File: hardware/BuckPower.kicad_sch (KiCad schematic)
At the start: 24 parts, among them Q401 NMOS, U401 SIC437A

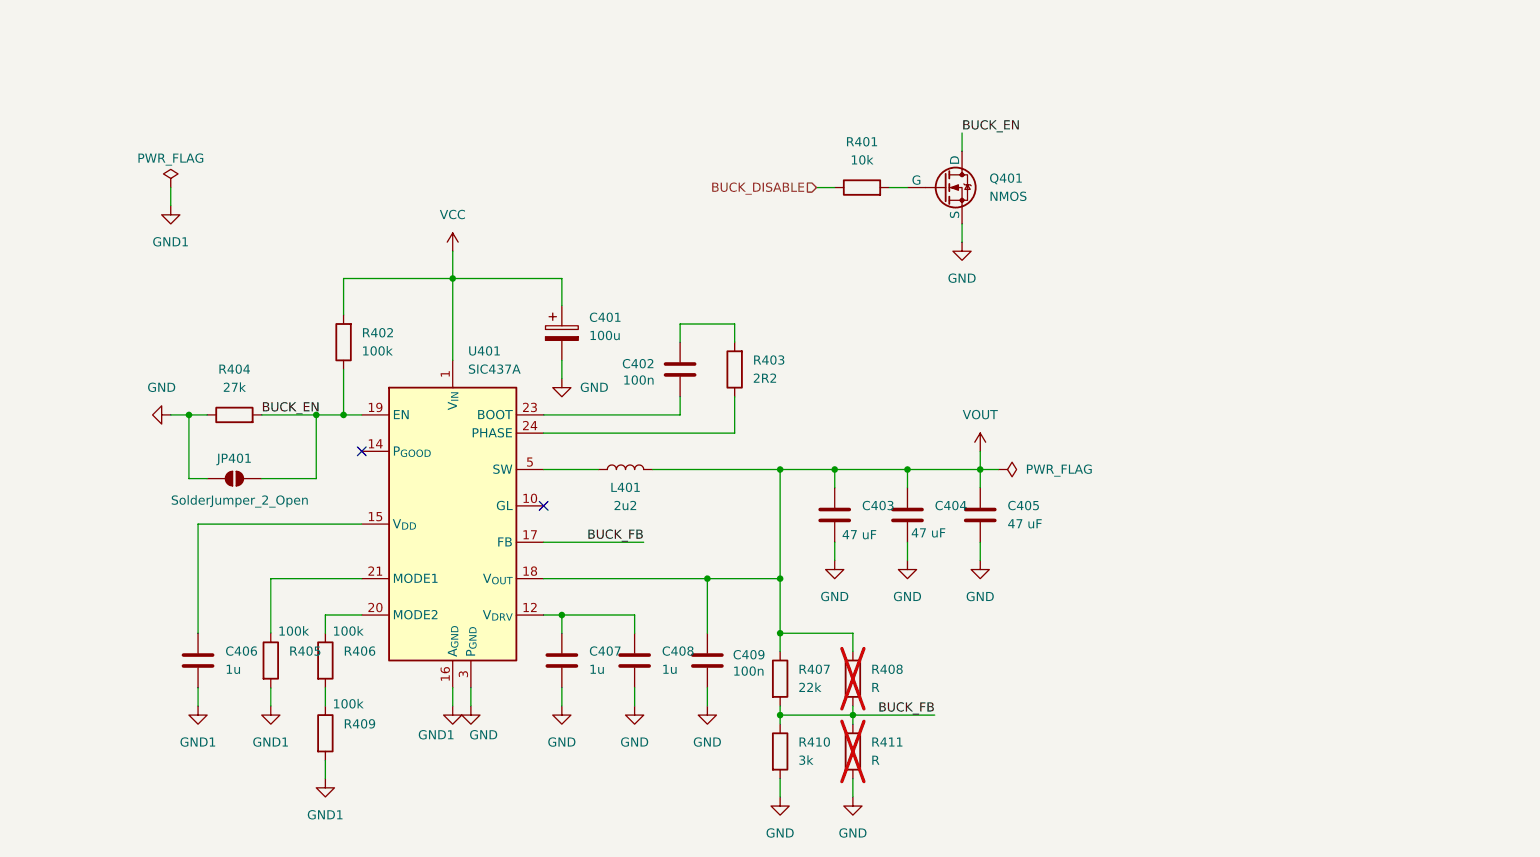
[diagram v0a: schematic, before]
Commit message: Optimized BOM and added netties
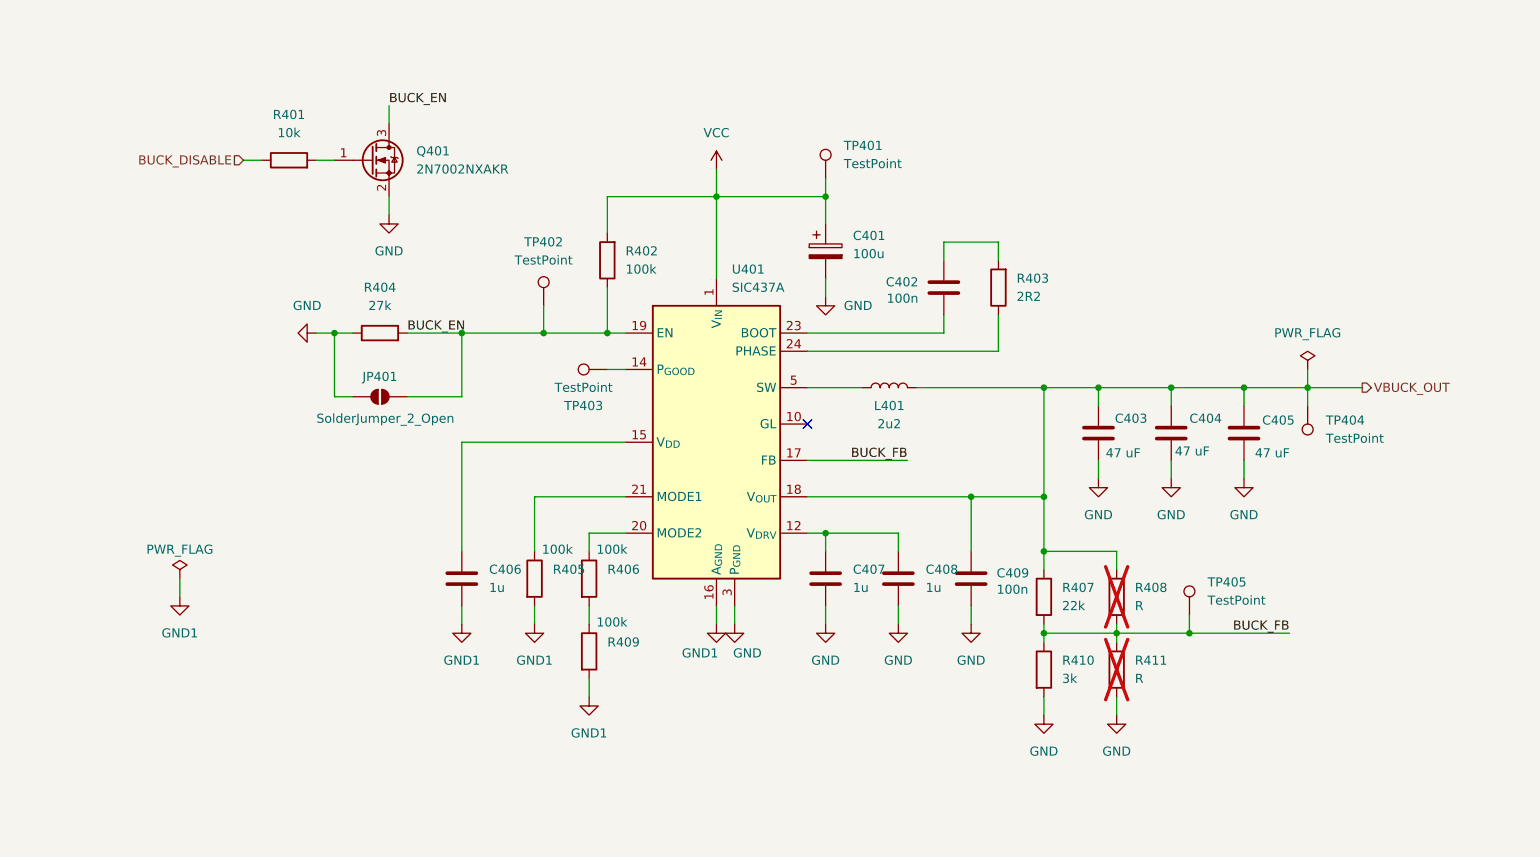
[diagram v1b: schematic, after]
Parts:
- removed Q401: NMOS, symbol Simulation_SPICE:NMOS
- added Q401: 2N7002NXAKR, Package_TO_SOT_SMD:SOT-23-3, symbol glowbuck:2N7002NXAKR
- added TP401, TP402, TP403, TP404, TP405: TestPoint, TestPoint:TestPoint_Pad_D1.0mm, symbol Connector:TestPoint
- L401: footprint (none) -> Inductor_SMD:L_Vishay_IHLP-6767; ManufacturerNumber (none) -> IHLP6767GZER2R2M01; MouserNumber (none) -> 70-IHLP6767GZER2R2M0
- R408, R411: now left out of the parts list
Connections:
- net BUCK_EN: now also Q401.3 (D), TP402.1
- net BUCK_FB: now also TP405.1
- net GND: now also Q401.2 (S)
- net VCC: now also TP401.1
- net at R401.2: now also Q401.1 (G)
- net at U401.14 (P_{GOOD}): now also TP403.1
- net VOUT renamed VBUCK_OUT
- net VBUCK_OUT: now also TP404.1
- no-connect marks 2 -> 1
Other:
- moved on the sheet: C401, C402, C403, C404, C405, C406, C407, C408, C409, JP401, L401, R401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

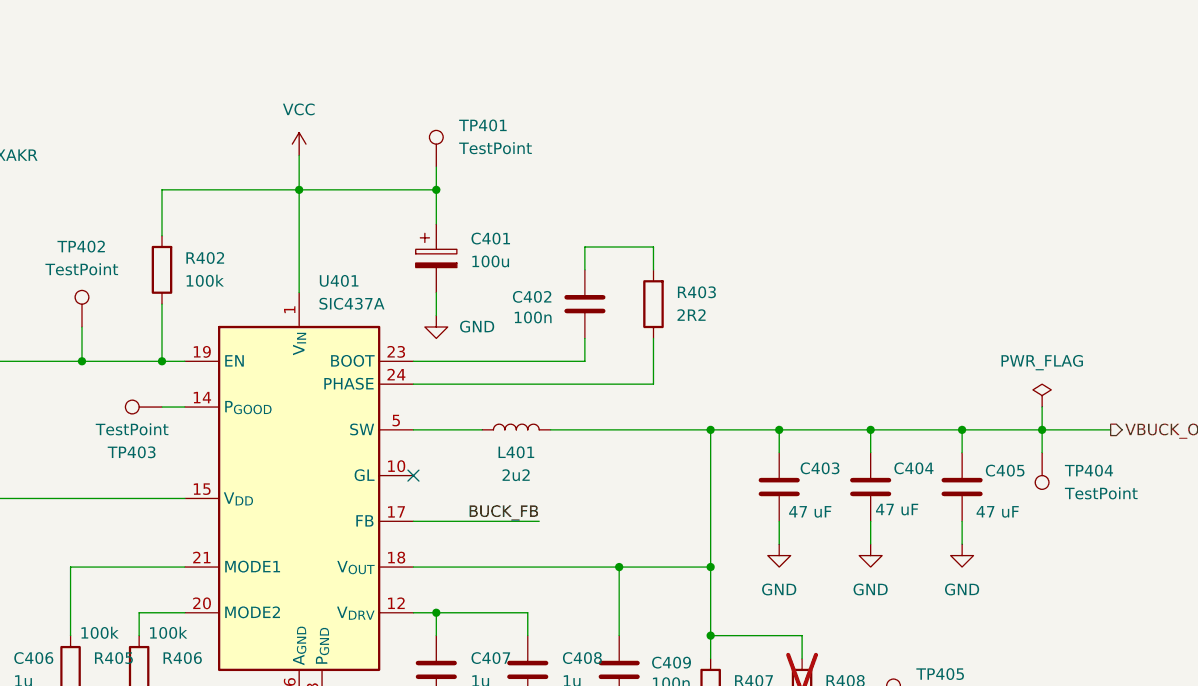
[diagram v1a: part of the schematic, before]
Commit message: Spring terminal, finalising PD settings, checking buck 10 A
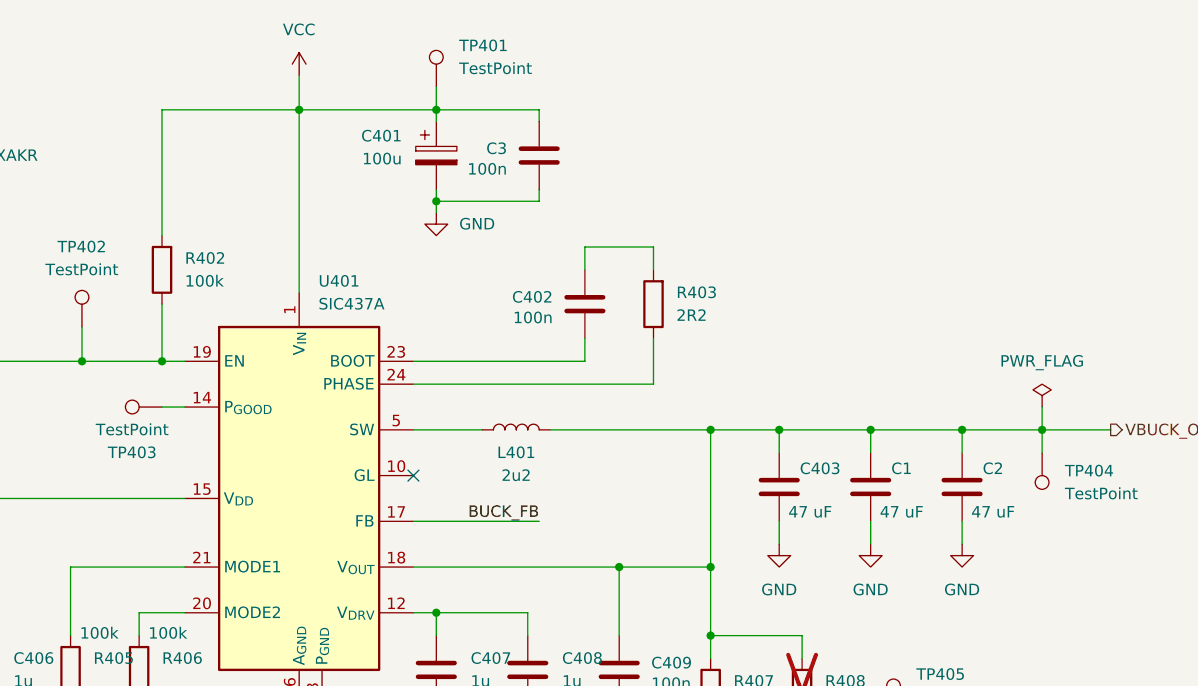
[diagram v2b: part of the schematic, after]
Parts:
- removed C404, C405: 47 uF, Capacitor_SMD:C_1210_3225Metric_Pad1.33x2.70mm_HandSolder, symbol Device:C
- added C1, C2: 47 uF, Capacitor_SMD:C_1210_3225Metric_Pad1.33x2.70mm_HandSolder, symbol Device:C
- added C3: 100n, Capacitor_SMD:C_0603_1608Metric_Pad1.08x0.95mm_HandSolder, symbol Device:C
- C403: ManufacturerNumber (none) -> GRM32ER71A476KE15L
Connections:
- net GND: now also C1.2, C2.2, C3.2
- net VBUCK_OUT: now also C1.1, C2.1
- net VCC: now also C3.1
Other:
- moved on the sheet: C401, TP401

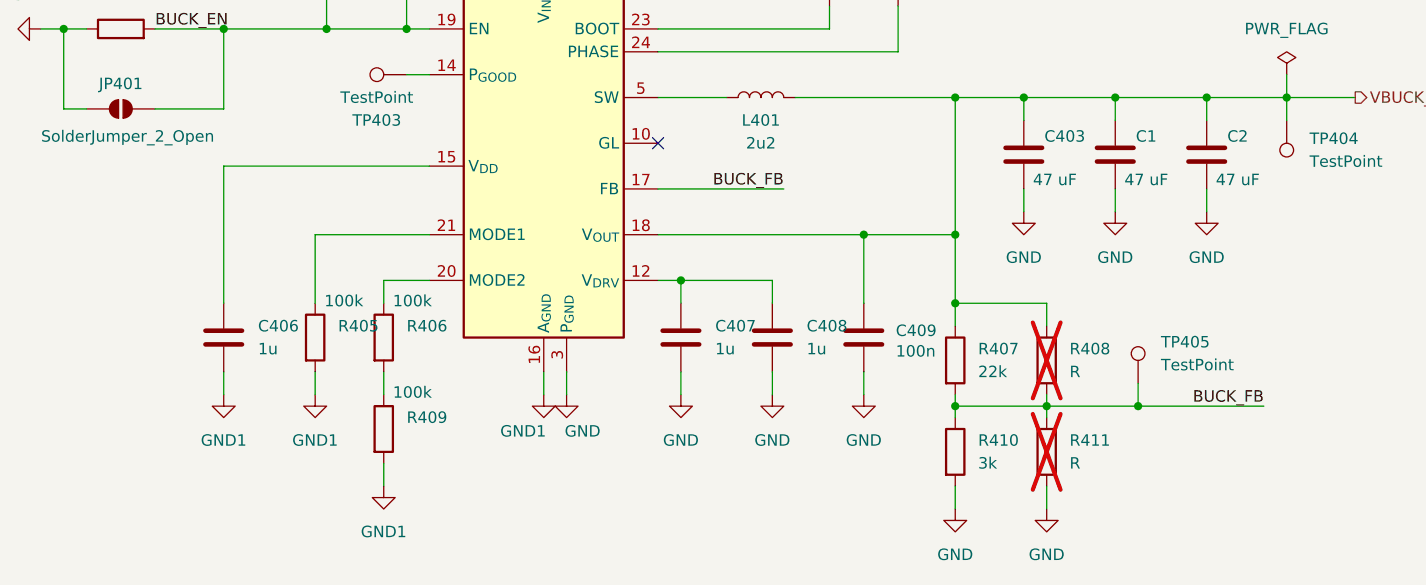
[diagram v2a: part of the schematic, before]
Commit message: Changed footprints to non hand solder option
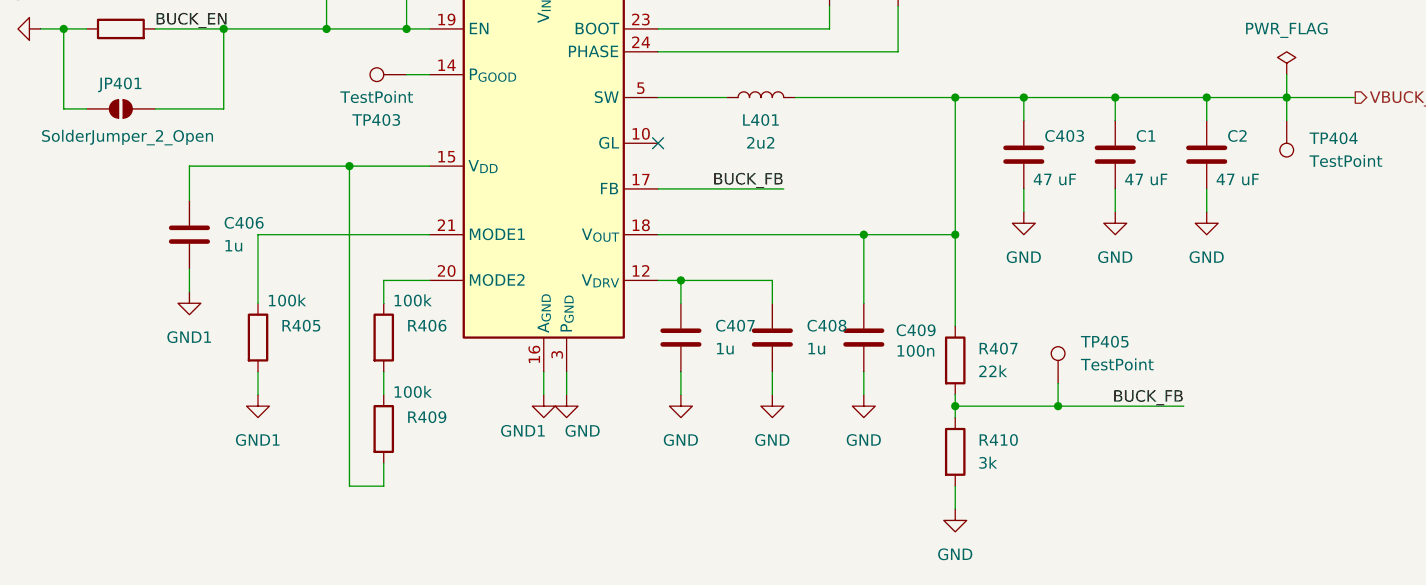
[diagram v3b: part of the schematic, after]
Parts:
- removed R408, R411: R, Resistor_SMD:R_0603_1608Metric_Pad0.98x0.95mm_HandSolder, symbol Device:R
- C1, C2, C403: footprint Capacitor_SMD:C_1210_3225Metric_Pad1.33x2.70mm_HandSolder -> Capacitor_SMD:C_1210_3225Metric
- C3, C402, C406, C407, C408, C409: footprint Capacitor_SMD:C_0603_1608Metric_Pad1.08x0.95mm_HandSolder -> Capacitor_SMD:C_0603_1608Metric
- R401, R402, R403, R404, R405, R406, R407, R409, R410: footprint Resistor_SMD:R_0603_1608Metric_Pad0.98x0.95mm_HandSolder -> Resistor_SMD:R_0603_1608Metric
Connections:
- net GND1: no longer R409.2
- net at C406.1, U401.15 (V_{DD}): now also R409.2
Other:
- moved on the sheet: C406, R405, TP405

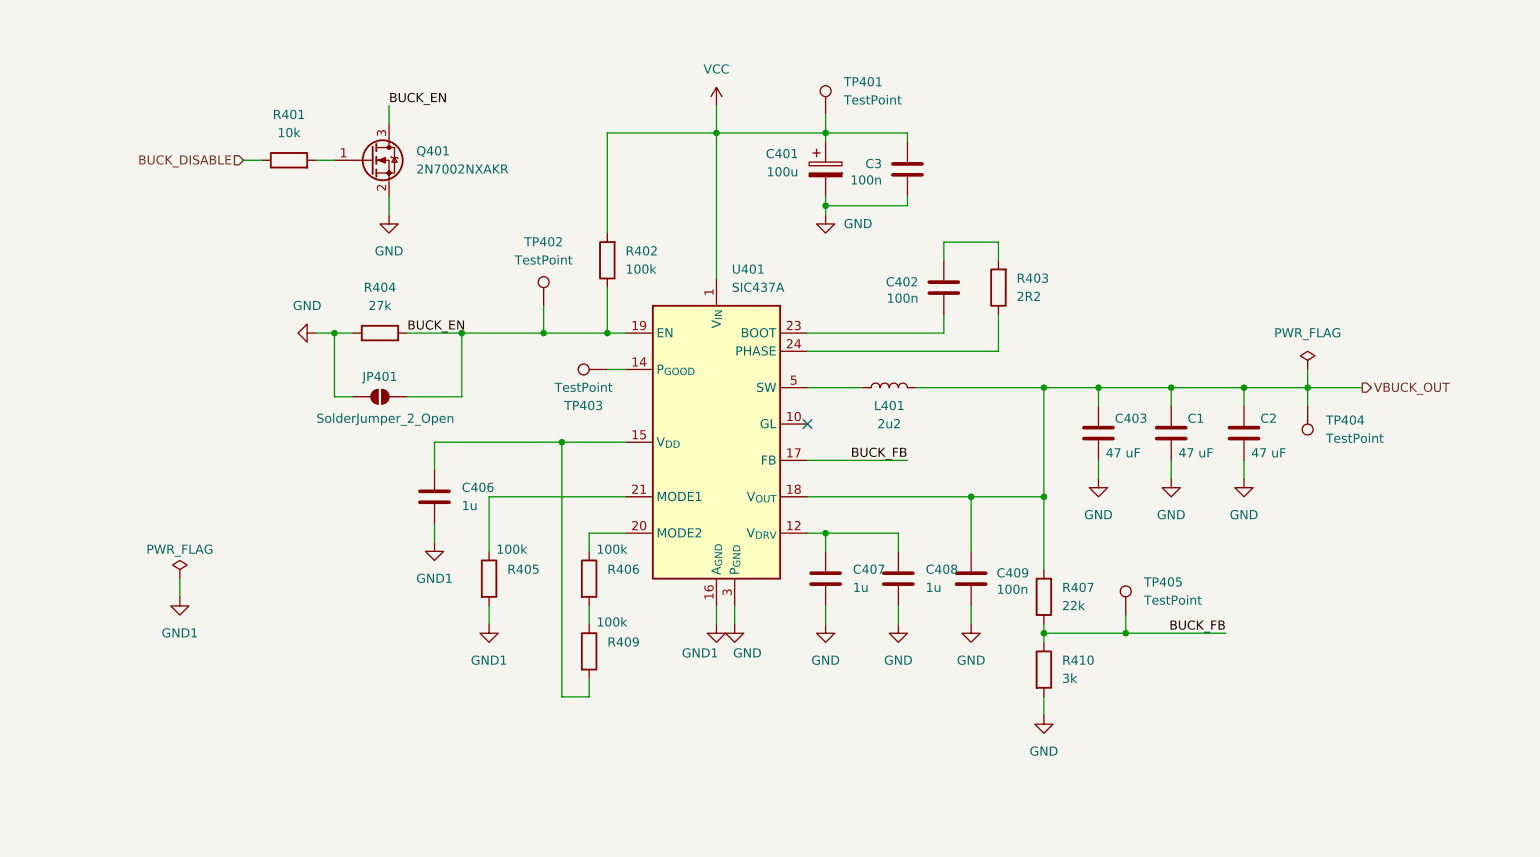
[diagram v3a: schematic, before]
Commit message: Colored nets and added optional current measurement
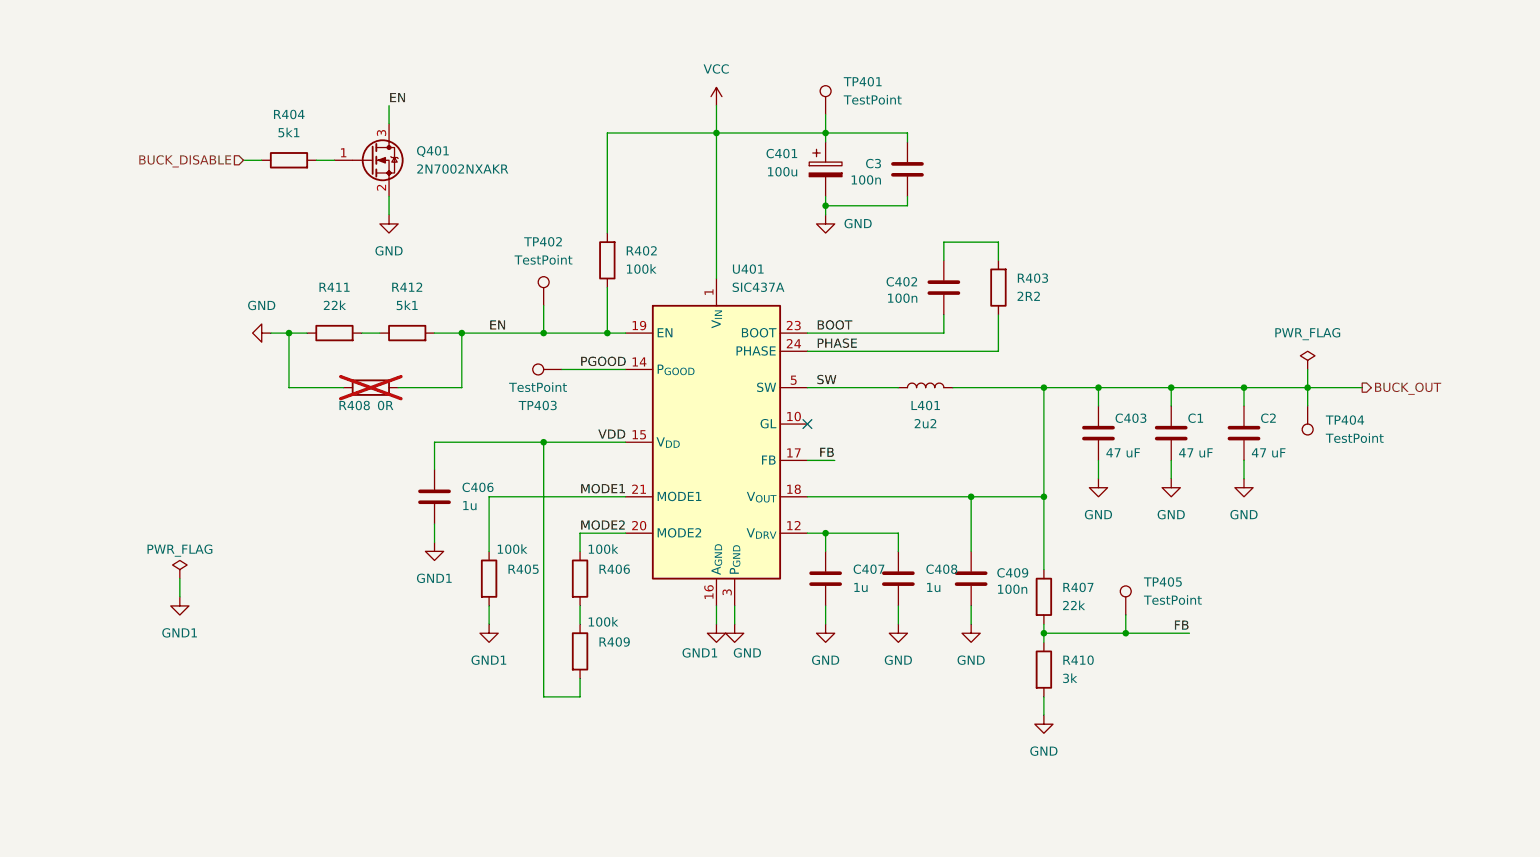
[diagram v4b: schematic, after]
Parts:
- removed JP401: SolderJumper_2_Open, Jumper:SolderJumper-2_P1.3mm_Open_Pad1.0x1.5mm, symbol Jumper:SolderJumper_2_Open
- removed R401: 10k, Resistor_SMD:R_0603_1608Metric, symbol Device:R
- added R408: 0R, Resistor_SMD:R_0603_1608Metric, symbol Device:R
- added R411: 22k, Resistor_SMD:R_0603_1608Metric, symbol Device:R
- added R412: 5k1, Resistor_SMD:R_0603_1608Metric, symbol Device:R
- R404: value 27k -> 5k1; MouserNumber (none) -> 652-CRT0603FZ1002ELF; now left out of the parts list
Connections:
- net BUCK_DISABLE: now also R404.1
- net GND: now also R408.2, R411.1; no longer R404.1
- net PHASE: now reaches R403.1, U401.24 (PHASE)
- net at Q401.1 (G): now also R404.2
- net MODE1: now reaches R405.1, U401.21 (MODE1)
- net MODE2: now reaches R406.1, U401.20 (MODE2)
- net SW: now reaches L401.1, U401.5 (SW), U401.6 (SW), U401.7 (SW), U401.8 (SW), U401.9 (SW)
- net PGOOD: now reaches TP403.1, U401.14 (P_{GOOD})
- net VDD: now reaches C406.1, R409.2, U401.15 (V_{DD})
- net BOOT: now reaches C402.2, U401.23 (BOOT)
- net BUCK_EN renamed EN
- net EN: now also R408.1, R412.2; no longer R404.2
- net BUCK_FB renamed FB
- net VBUCK_OUT renamed BUCK_OUT
- new net: R411.2, R412.1
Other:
- moved on the sheet: L401, R406, R409, TP403
